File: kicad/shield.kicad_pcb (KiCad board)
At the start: 4 copper layers, 56.5 x 42 mm, 35 parts, among them J1 Conn_01x11, J2 Conn_01x12, J3 Conn_01x24, Q1 ZXMN3B01F, Q39 Q_PNP_BEC, SW1 SW_Push, SW2 SW_Push, SW3 SW_Push, SW4 SW_Push

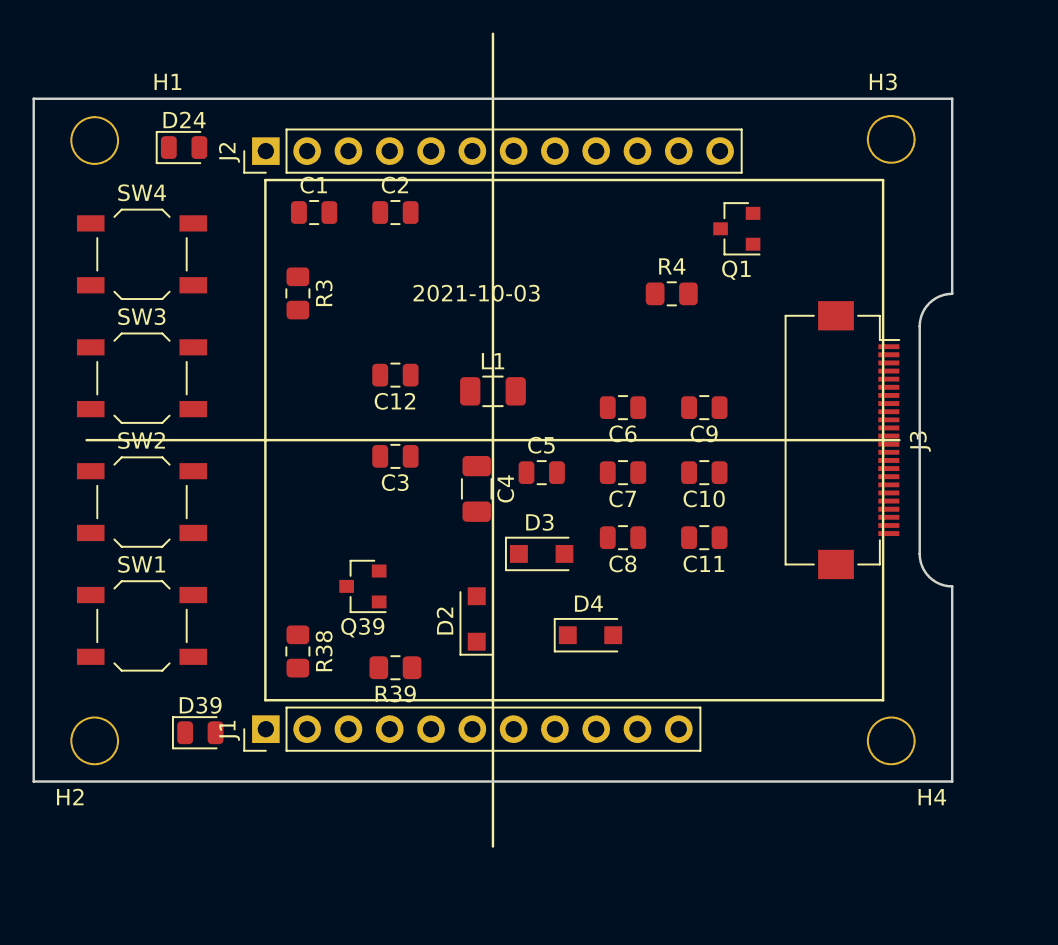
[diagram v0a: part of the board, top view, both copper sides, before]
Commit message: did routing, ready to be tested
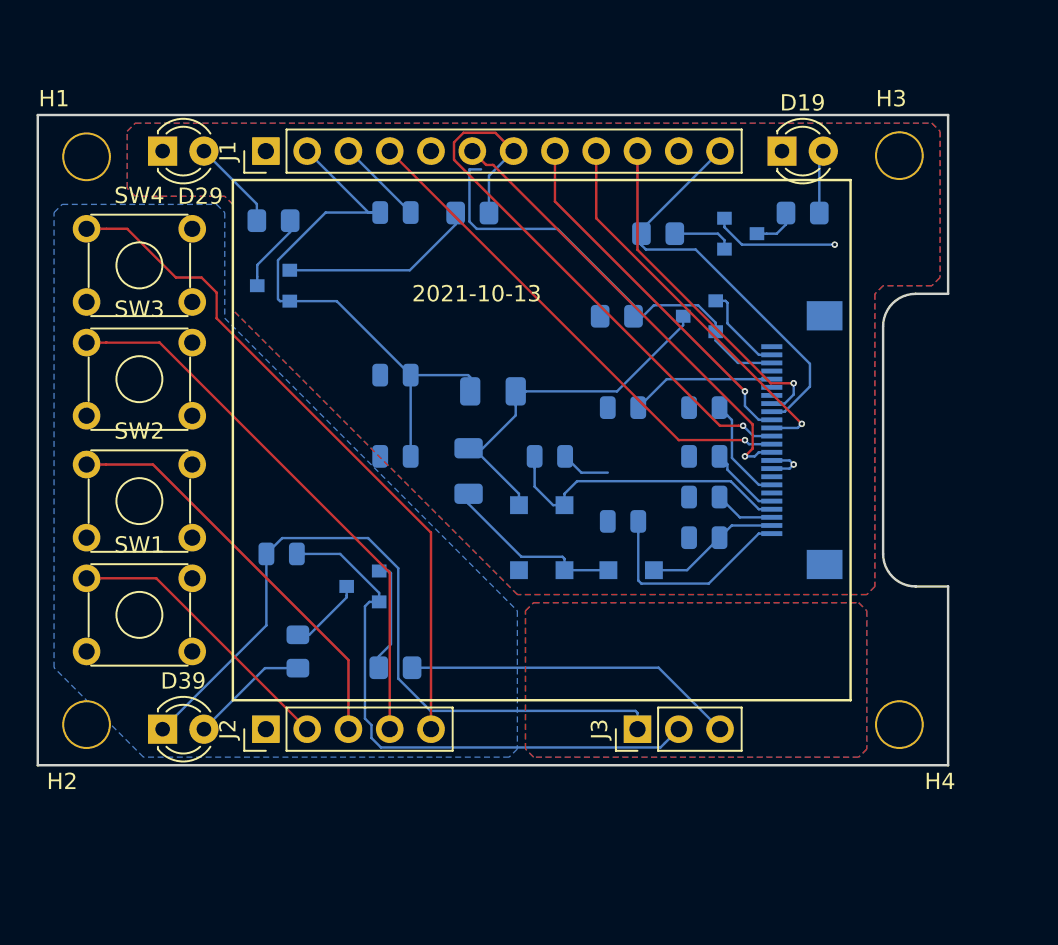
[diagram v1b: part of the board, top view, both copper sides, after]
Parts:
- removed D24: LED, LED_SMD:LED_0805_2012Metric
- removed the J1 at (-14.0, 17.8)
- removed R3: 1K, Resistor_SMD:R_0805_2012Metric_Pad1.15x1.40mm_HandSolder
- added D19: LED, LED_THT:LED_D3.0mm, F.Cu at (17.8, -17.8)
- added D29: LED, LED_THT:LED_D3.0mm, F.Cu at (-20.3, -17.8)
- added J2: Conn_01x05, Connector_PinHeader_2.54mm:PinHeader_1x05_P2.54mm_Vertical, F.Cu at (-14.0, 17.8)
- added J3: Conn_01x03, Connector_PinHeader_2.54mm:PinHeader_1x03_P2.54mm_Vertical, F.Cu at (8.89, 17.8)
- added Q19: Q_PNP_BEC, Package_TO_SOT_SMD:SOT-23, B.Cu at (15.2, -12.7)
- added Q29: Q_PNP_BEC, Package_TO_SOT_SMD:SOT-23, B.Cu at (-13.5, -9.50)
- added R18: 220, Resistor_SMD:R_0805_2012Metric_Pad1.15x1.40mm_HandSolder, B.Cu at (19.1, -14.0)
- added R19: 1K, Resistor_SMD:R_0805_2012Metric_Pad1.15x1.40mm_HandSolder, B.Cu at (10.2, -12.7)
- added R28: 220, Resistor_SMD:R_0805_2012Metric_Pad1.15x1.40mm_HandSolder, B.Cu at (-13.5, -13.5)
- added R29: 1K, Resistor_SMD:R_0805_2012Metric_Pad1.15x1.40mm_HandSolder, B.Cu at (-1.27, -14.0)
- C10, C11, C12, C2, C3, C4, C5, C6, C7, C8, C9, D2, D3, D4, L1, Q1, Q39, R38, R39, R4: moved to B.Cu
- C39: renamed from C1; moved to B.Cu
- D39: footprint LED_SMD:LED_0805_2012Metric -> LED_THT:LED_D3.0mm
- J4: renamed from J3; moved to B.Cu
- SW1, SW2, SW3, SW4: footprint Button_Switch_SMD:SW_SPST_TL3342 -> Button_Switch_THT:SW_TH_Tactile_Omron_B3F-10xx
- moved C39 21.1 mm to (-13.0, 7.00), turned to 180 degrees
- moved Q1 5.85 mm to (12.7, -7.62)
- moved C7 5.10 mm to (13.0, 1.00)
- moved D2 5.00 mm to (3.00, 8.00), turned to 0 degrees
- moved D4 4.72 mm to (8.50, 8.00)
- moved SW1 4.50 mm to (-25.0, 8.50)
- moved SW2 4.12 mm to (-25.0, 1.50)
- moved SW3 4.05 mm to (-25.0, -6.00)
- moved SW4 3.75 mm to (-25.0, -13.0)
- moved R4 3.65 mm to (7.62, -7.62)
- moved J4 3.50 mm to (19.0, 0.00)
- moved D3 3.00 mm to (3.00, 4.00), turned to 180 degrees
- moved D39 2.33 mm to (-20.3, 17.8)
- moved C10 1.50 mm to (13.0, 3.50)
- moved C4 1.21 mm to (-1.50, 1.90)
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- renumbered J2 to J1
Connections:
- C39 pad 1: /P5V -> /LED_Power
- C39 pad 2: GND -> /LED_GND
- D39 pad 1: GND -> /LED_GND
- J1 pad 1: /P5V -> (no net)
- Q39 pad 2: /P3V3 -> /LED_Power
- R39 pad 1: /GPIO16_Satus_LED -> /GPIO16_Satus_LED_N
- SW1 pad 2: GND -> /SW_GND
- SW2 pad 2: GND -> /SW_GND
- SW3 pad 2: GND -> /SW_GND
- SW4 pad 2: GND -> /SW_GND
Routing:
- net /P3V3: track 0.00 -> 46.3 mm, vias 0 -> 2
- net /LED_GND: track 0.00 -> 46.1 mm
- net /GPIO17_J1: track 0.00 -> 41.9 mm
- net /GPIO8_TFT_CS: track 0.00 -> 36.5 mm, vias 0 -> 1
- net /LED_Power: track 0.00 -> 35.5 mm
- net /GPIO27_J1: track 0.00 -> 34.1 mm
- net /GPIO11_SCLK: track 0.00 -> 31.0 mm, vias 0 -> 1
- net /GPIO10_MOSI: track 0.00 -> 28.1 mm, vias 0 -> 1
- net Net-(J4-Pad3): track 0.00 -> 27.7 mm
- net /GPIO6_BUSY_N: track 0.00 -> 25.6 mm
- net /GPIO22_J1: track 0.00 -> 25.3 mm
- net /GPIO25_DATA_OR_CMD: track 0.00 -> 24.0 mm, vias 0 -> 1
- net Net-(C4-Pad1): track 0.00 -> 22.7 mm
- net /GPIO24_RESET: track 0.00 -> 22.5 mm, vias 0 -> 1
- net /GPIO7_BS: track 0.00 -> 21.4 mm, vias 0 -> 1
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- added copper zone on B.Cu, net /LED_GND
- added copper zone on F.Cu, net /LED_Power
- added copper zone on F.Cu, net /P3V3
- added copper zone on B.Cu, net /SW_GND
- added copper zone on B.Cu, net GND
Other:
- board size 56.5 x 42 mm -> 56 x 40 mm
- board text added: "2021-10-13"
- board text removed: "2021-10-03"
- board text removed: "If you want to use an SMT 40-pin header, please move the top edge up by 0.5mm and locate the header in the same location as the current TH part."
- board text removed: "This is a HAT compatible PCB starting design based on the official Raspberry Pi specs at: https://github.com/raspberrypi/hats/blob/master/designguide.md Currently the camera slot and display cutout are not here. See the schematic for the details on the EEPROM and power setup. This board does have the correct components for powering the Pi via the HAT. If you need the Pi to provide 5V or 3.3V, ple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"

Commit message: added power LED
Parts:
- added D99: LED, LED_THT:LED_D3.0mm, F.Cu at (16.5, 17.8)
- added R98: 1K, Resistor_SMD:R_0805_2012Metric_Pad1.15x1.40mm_HandSolder, B.Cu at (17.9, 12.4)
- moved D19 1.27 mm to (16.5, -17.8)
- moved D29 1.27 mm to (-19.1, -17.8)
- moved D39 1.27 mm to (-19.1, 17.8)
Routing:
- net GND: track 8.43 -> 147.9 mm
- net Net-(J4-Pad3): track 27.7 -> 11.6 mm
- net /P3V3: track 46.3 -> 61.7 mm, vias 2 -> 3
- net Net-(D99-Pad2): track 0.00 -> 4.83 mm
- net /GPIO10_MOSI: track 28.1 -> 30.7 mm, vias 1 -> 2
- net Net-(C5-Pad1): track 18.7 -> 19.9 mm, vias 0 -> 3
- net Net-(C9-Pad1): track 6.55 -> 7.19 mm, vias 0 -> 2
- net Net-(D39-Pad2): track 7.34 -> 6.81 mm
- net Net-(D29-Pad2): track 5.63 -> 5.10 mm
- net /LED_GND: track 46.1 -> 45.6 mm
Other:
- copper layers 4 -> 2

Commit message: replaced power LED with a PWM LED
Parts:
- removed D99: LED, LED_THT:LED_D3.0mm
- removed R98: 1K, Resistor_SMD:R_0805_2012Metric_Pad1.15x1.40mm_HandSolder
- added D49: LED, LED_THT:LED_D3.0mm, F.Cu at (17.8, 17.8)
- added Q49: Q_PNP_BEC, Package_TO_SOT_SMD:SOT-23, B.Cu at (14.0, 12.7)
- added R48: 220, Resistor_SMD:R_0805_2012Metric_Pad1.15x1.40mm_HandSolder, B.Cu at (19.1, 14.0)
- added R49: 1K, Resistor_SMD:R_0805_2012Metric_Pad1.15x1.40mm_HandSolder, B.Cu at (19.1, 11.4)
- moved C3 2.25 mm to (-5.20, -1.10)
- moved D19 1.27 mm to (17.8, -17.8)
- moved D29 1.27 mm to (-20.3, -17.8)
- moved D39 1.27 mm to (-20.3, 17.8)
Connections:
- J1 pad 11: (no net) -> /GPIO12_PWM0_BACKLIGHT
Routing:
- net GND: track 147.9 -> 83.2 mm
- net /GPIO12_PWM0_BACKLIGHT: track 0.00 -> 35.9 mm, vias 0 -> 1
- net /GPIO8_TFT_CS: track 36.5 -> 29.0 mm
- net /P3V3: track 61.7 -> 54.3 mm
- net Net-(Q49-Pad3): track 0.00 -> 6.34 mm
- net Net-(D99-Pad2): track 4.83 -> 0.00 mm
- net Net-(D49-Pad2): track 0.00 -> 3.91 mm
- net Net-(Q49-Pad1): track 0.00 -> 3.19 mm
- net Net-(C5-Pad1): track 19.9 -> 17.8 mm, vias 3 -> 2
- net /GPIO10_MOSI: track 30.7 -> 28.8 mm, vias 2 -> 1
- net Net-(J4-Pad3): track 11.6 -> 10.9 mm
- net Net-(D39-Pad2): track 6.81 -> 7.34 mm
- net Net-(D29-Pad2): track 5.10 -> 5.63 mm
- net /LED_GND: track 45.6 -> 46.1 mm
- net /GPIO6_BUSY_N: vias 0 -> 2
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- removed copper zone on B.Cu, net /LED_GND
- removed copper zone on F.Cu, net /LED_Power
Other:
- outline, holes or cut-outs redrawn
- board text added: "2021-10-14"
- board text removed: "2021-10-13"
